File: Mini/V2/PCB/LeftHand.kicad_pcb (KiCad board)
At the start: 2 copper layers, 155.9 x 99.3 mm, 30 parts

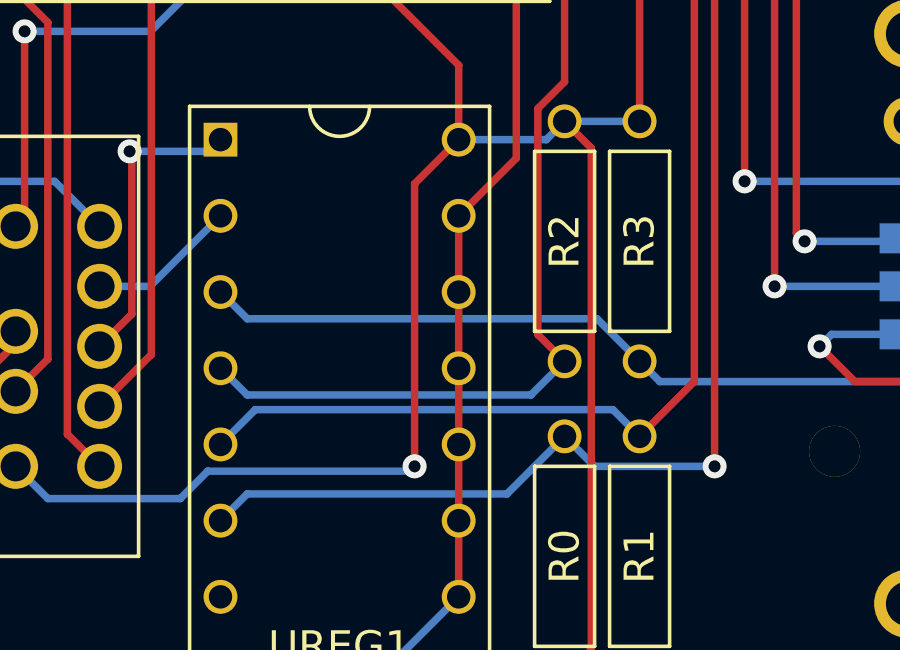
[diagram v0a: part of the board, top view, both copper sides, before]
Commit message: Updating LH PCB register to read 01 for register[4..5] and RH to read 10.  V1 will read as 00 for controller logic backward compatibility.
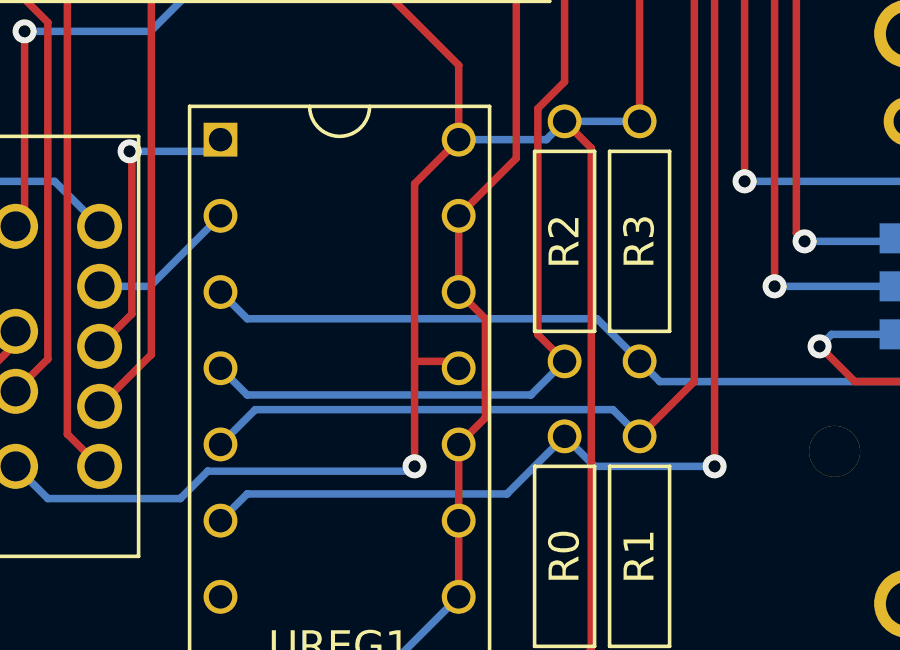
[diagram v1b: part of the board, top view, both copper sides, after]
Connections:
- UREG1 pad 13: GND -> VCC
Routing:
- net VCC: track 630.8 -> 632.4 mm
- net GND: track 630.8 -> 631.6 mm
